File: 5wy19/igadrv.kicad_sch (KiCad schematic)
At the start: 0 parts

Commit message: Further progress on MCU and connected circuits
Mostly sensors, knock control, some pins from the IO drivers and the unknown AMIS chip
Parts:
- added Q24, Q3: ISL9V5036S3ST, symbol Device:Q_NIGBT_GCE
- added R107, R29: 1k, symbol Device:R_Small
- added R60, R76: 31.6k, symbol Device:R_Small
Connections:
- new net: Q3.1 (G), R29.1
- new net: Q24.1 (G), R107.2
- new net GND: Q24.3 (E), Q3.3 (E)
- new net IGN 2/3: R107.1
- new net IGN 2/3 MON: R76.1
- new net IGN 4/1: R29.2
- new net IGN 4/1 MON: R60.1
- new net Ign. Coil 1&4: Q24.2 (C), Q3.2 (C), R60.2, R76.2

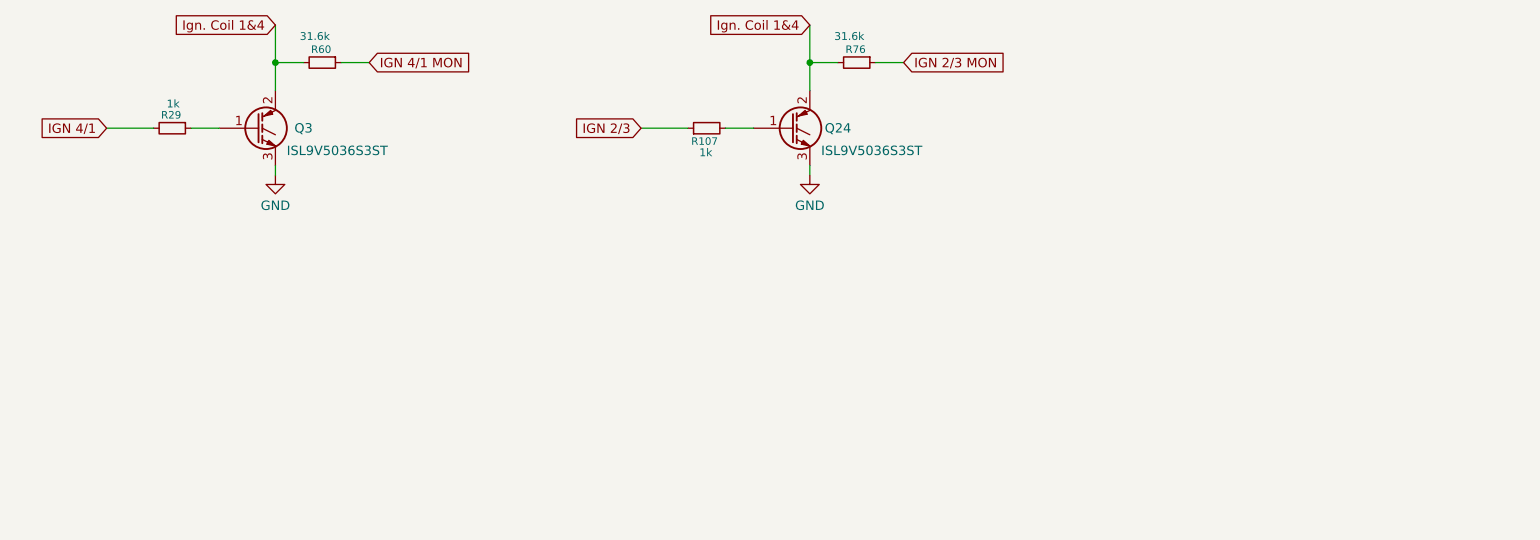
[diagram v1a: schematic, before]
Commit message: Finished most of the subsystems
-- MCU finished
-- Flash finished
-- Power Supply finished
-- I/O Drivers finished
-- CANBUS finished
-- Knock Control finished
-- Connector finished
-- Ignition Driver finished
-- Sensor Logic mostly finished
-- Logic ICs need some work
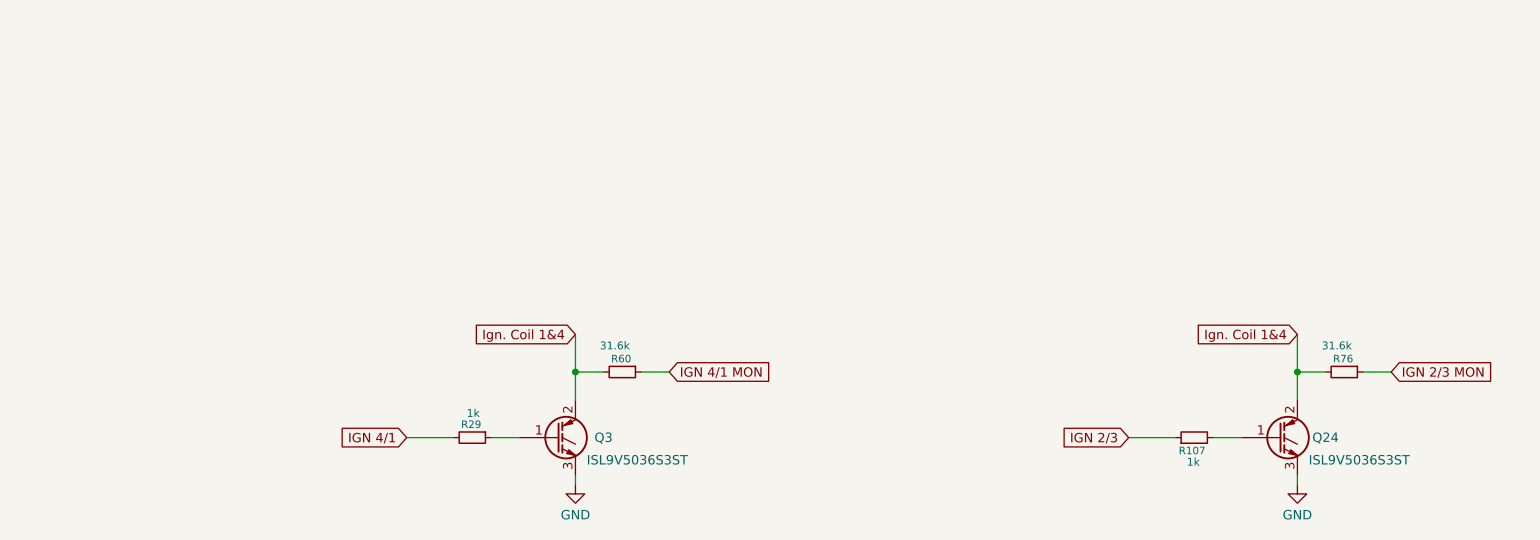
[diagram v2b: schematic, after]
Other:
- title: (none) -> SMIK43 5WY19 Rev. Eng
- moved on the sheet: Q24, Q3, R107, R29, R60, R76

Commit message: Final schematic (except maybe some oversights)
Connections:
- net Ign. Coil 1&4: no longer Q24.2 (C), R76.2
- new net Ign. Coil 2&3: Q24.2 (C), R76.2
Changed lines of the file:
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@@
 		)
 	)
-	(global_label "Ign. Coil 1&4"
+	(global_label "Ign. Coil 2&3"
 		(shape input)
 		(at 205.74 81.28 180)
